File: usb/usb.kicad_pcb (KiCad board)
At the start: 4 copper layers, 40 x 17.5 mm, 14 parts, among them J101 JAE_DX07S016JA3, J102 2x05_Horizontal

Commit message: Update usb + link-poe
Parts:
- C101: footprint Capacitor_SMD:C_0603_1608Metric -> V2_Capacitor_SMD:C_0603
- R101, R102: footprint Resistor_SMD:R_0603_1608Metric -> V2_Resistor_SMD:R_0603
- moved ICON101 13.6 mm to (139.5, 102.2)
- moved H102 5.01 mm to (148.0, 106.2)
- moved J102 5.01 mm to (153.0, 106.2)
- moved PLUG101 5.01 mm to (153.0, 106.2)
- moved FID103 5.00 mm to (161.0, 114.0)
- moved INFO101 3.50 mm to (124.5, 114.2)
- moved INFO102 2.51 mm to (139.5, 113.5)
- moved C101 2.50 mm to (139.5, 106.2)
- moved H101 0.25 mm to (131.0, 106.2)
- moved J101 0.25 mm to (122.0, 106.2)
- moved R101 0.25 mm to (129.0, 101.5)
- moved R102 0.25 mm to (129.0, 111.0)
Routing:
- net /USB+: track 24.5 -> 30.3 mm
- net /USB-: track 31.2 -> 36.7 mm
- net GND: vias 10 -> 29
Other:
- board size 40 x 17.5 mm -> 45 x 17.5 mm

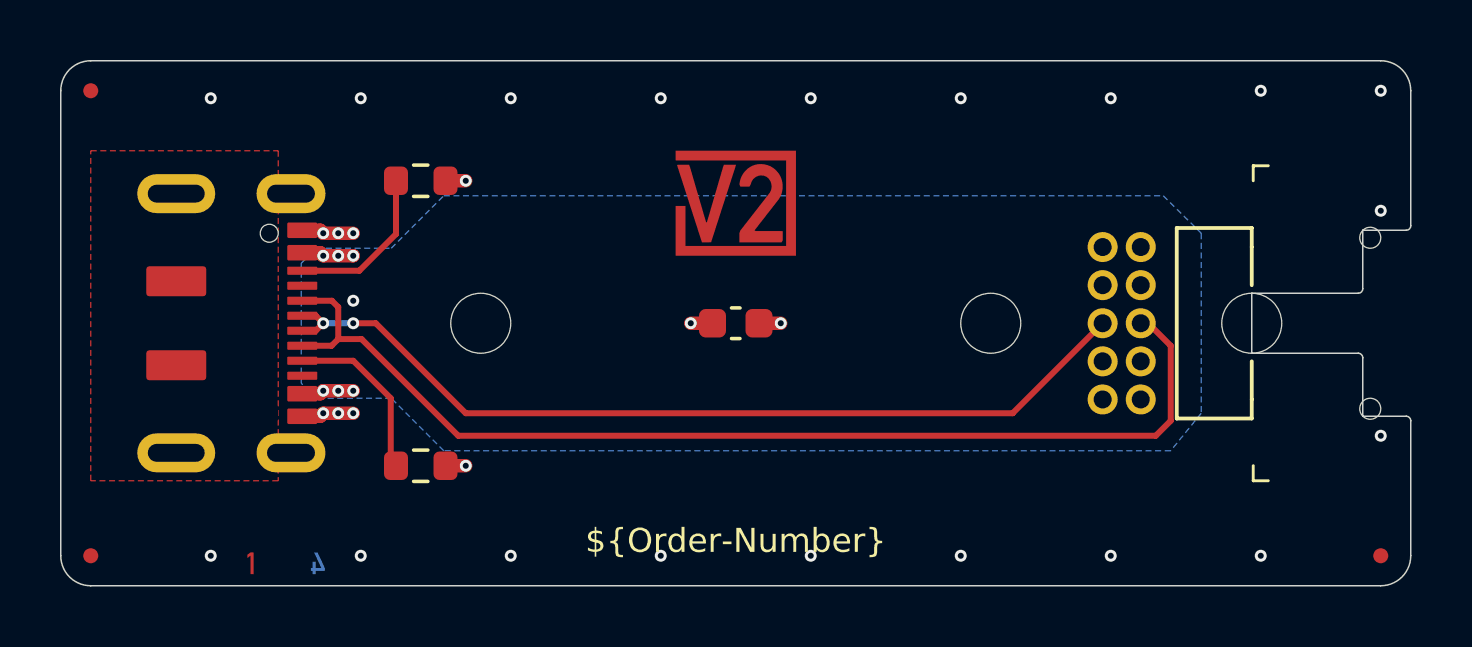
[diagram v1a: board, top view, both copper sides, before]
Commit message: Update power symbols
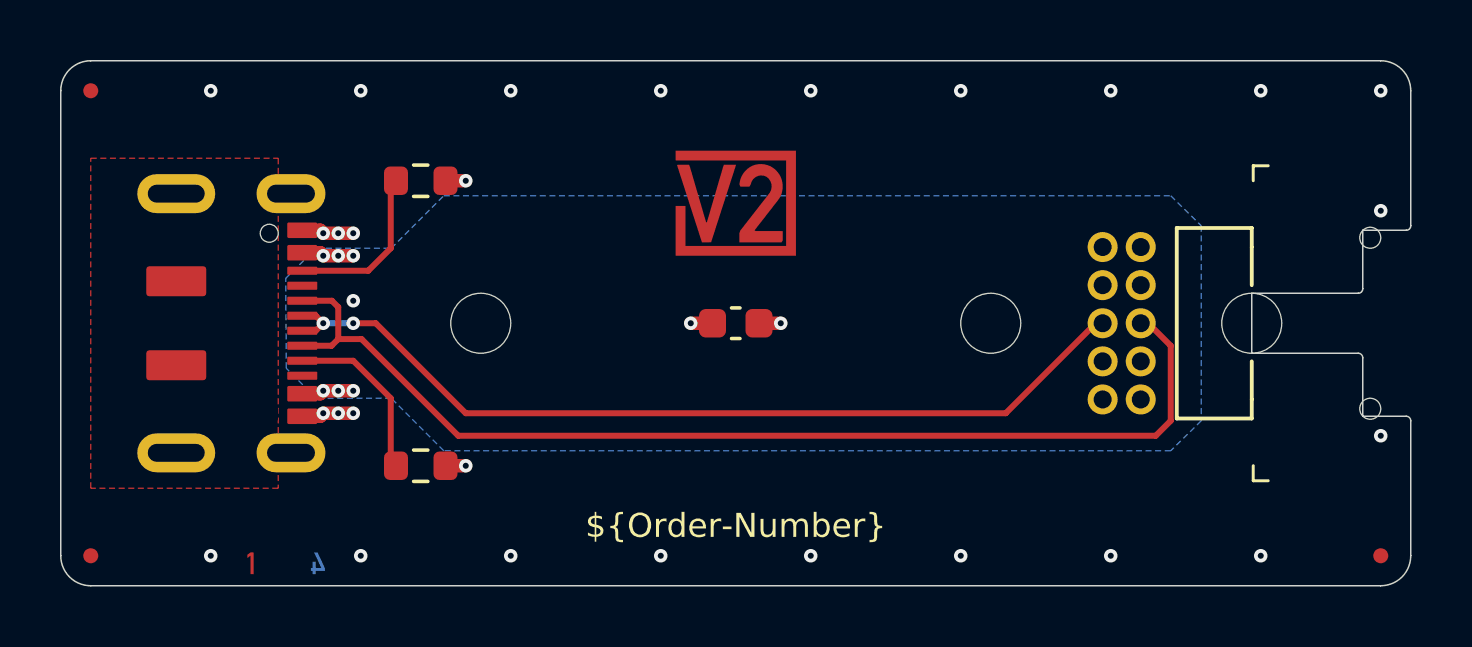
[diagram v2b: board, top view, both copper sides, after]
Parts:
- FID101, FID102, FID103: value Fiducial -> Fiducial_Paste
- INFO102: value ORDER-NUMBER -> Order_Number
- J101: value JAE_DX07S016JA3 -> DX07S016JA3
- moved INFO102 0.50 mm to (139.5, 113.0)
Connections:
- net USB-Shield renamed Shield

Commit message: Fix WAGOs
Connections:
- net VBUS renamed +VBUS
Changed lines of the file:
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@@
 	(net 0 "")
 	(net 1 "GND")
-	(net 2 "VBUS")
+	(net 2 "+VBUS")
 	(net 3 "unconnected-(J101-SBU1-PadA8)")
 	(net 4 "unconnected-(J101-SBU2-PadB8)")
@@
 		)
 		(fp_rect
-			(start -1.48 -0.73)
-			(end 1.48 0.73)
+			(start -1.23 -0.73)
+			(end 1.23 0.73)
 			(stroke
 				(width 0.05)
@@
 		)
 		(pad "1" smd roundrect
-			(at -0.825 0)
-			(size 0.8 0.95)
+			(at -0.75 0)
+			(size 0.75 0.95)
 			(layers "F.Cu" "F.Mask" "F.Paste")
-			(roundrect_rratio 0.25)
+			(roundrect_rratio 0.1333333333)
 			(net 9 "/USB-CC2")
 			(pintype "passive")
 		)
 		(pad "2" smd roundrect
-			(at 0.825 0)
-			(size 0.8 0.95)
+			(at 0.75 0)
+			(size 0.75 0.95)
 			(layers "F.Cu" "F.Mask" "F.Paste")
-			(roundrect_rratio 0.25)
+			(roundrect_rratio 0.1333333333)
 			(net 1 "GND")
 			(pintype "passive")
@@
 			)
 		)
+		(pad "" smd roundrect
+			(at -3.1 -3.05 270)
+			(size 0.45 1)
+			(layers "F.Paste")
+			(roundrect_rratio 0.1)
+		)
 		(pad "" np_thru_hole circle
 			(at -3 -1.95 270)
@@
 			(layers "*.Cu" "*.Mask")
 		)
+		(pad "" smd roundrect
+			(at -2.35 -3.05 270)
+			(size 0.45 1)
+			(layers "F.Paste")
+			(roundrect_rratio 0.1)
+		)
+		(pad "" smd roundrect
+			(at 2.35 -3.05 270)
+			(size 0.45 1)
+			(layers "F.Paste")
+			(roundrect_rratio 0.1)
+		)
 		(pad "" np_thru_hole oval
 			(at 3 -1.95 270)
@@
 			(layers "*.Cu" "*.Mask")
 		)
+		(pad "" smd roundrect
+			(at 3.1 -3.05 270)
+			(size 0.45 1)
+			(layers "F.Paste")
+			(roundrect_rratio 0.1)
+		)
 		(pad "A5" smd roundrect
 			(at -1.75 -3.05 270)
@@
 			(at -3.1 -3.05 270)
 			(size 0.52 1)
-			(layers "F.Cu" "F.Mask" "F.Paste")
+			(layers "F.Cu" "F.Mask")
 			(roundrect_rratio 0.1)
 			(net 1 "GND")
@@
 			(at 3.1 -3.05 270)
 			(size 0.52 1)
-			(layers "F.Cu" "F.Mask" "F.Paste")
+			(layers "F.Cu" "F.Mask")
 			(roundrect_rratio 0.1)
 			(net 1 "GND")
@@
 			(at -2.35 -3.05 270)
 			(size 0.52 1)
-			(layers "F.Cu" "F.Mask" "F.Paste")
+			(layers "F.Cu" "F.Mask")
 			(roundrect_rratio 0.1)
-			(net 2 "VBUS")
+			(net 2 "+VBUS")
 			(pinfunction "VBUS")
 			(pintype "passive")
@@
 			(at 2.35 -3.05 270)
 			(size 0.52 1)
-			(layers "F.Cu" "F.Mask" "F.Paste")
+			(layers "F.Cu" "F.Mask")
 			(roundrect_rratio 0.1)
-			(net 2 "VBUS")
+			(net 2 "+VBUS")
 			(pinfunction "VBUS")
 			(pintype "passive")
@@
 		)
 		(fp_rect
-			(start -1.48 -0.73)
-			(end 1.48 0.73)
+			(start -1.23 -0.73)
+			(end 1.23 0.73)
 			(stroke
 				(width 0.05)
@@
 		)
 		(pad "1" smd roundrect
-			(at -0.775 0 180)
-			(size 0.9 0.95)
+			(at -0.7 0 180)
+			(size 0.7 0.8)
 			(layers "F.Cu" "F.Mask" "F.Paste")
-			(roundrect_rratio 0.25)
-			(net 2 "VBUS")
+			(roundrect_rratio 0.1428571429)
+			(net 2 "+VBUS")
 			(pintype "passive")
 		)
 		(pad "2" smd roundrect
-			(at 0.775 0 180)
-			(size 0.9 0.95)
+			(at 0.7 0 180)
+			(size 0.7 0.8)
 			(layers "F.Cu" "F.Mask" "F.Paste")
-			(roundrect_rratio 0.25)
+			(roundrect_rratio 0.1428571429)
 			(net 1 "GND")
 			(pintype "passive")
@@
 		)
 		(fp_rect
-			(start -1.48 -0.73)
-			(end 1.48 0.73)
+			(start -1.23 -0.73)
+			(end 1.23 0.73)
 			(stroke
 				(width 0.05)
@@
 		)
 		(pad "1" smd roundrect
-			(at -0.825 0)
-			(size 0.8 0.95)
+			(at -0.75 0)
+			(size 0.75 0.95)
 			(layers "F.Cu" "F.Mask" "F.Paste")
-			(roundrect_rratio 0.25)
+			(roundrect_rratio 0.1333333333)
 			(net 8 "/USB-CC1")
 			(pintype "passive")
 		)
 		(pad "2" smd roundrect
-			(at 0.825 0)
-			(size 0.8 0.95)
+			(at 0.75 0)
+			(size 0.75 0.95)
 			(layers "F.Cu" "F.Mask" "F.Paste")
-			(roundrect_rratio 0.25)
+			(roundrect_rratio 0.1333333333)
 			(net 1 "GND")
 			(pintype "passive")
@@
 			(keep_end_layers yes)
 			(zone_layer_connections)
-			(net 2 "VBUS")
+			(net 2 "+VBUS")
 			(pinfunction "Pin_4")
 			(pintype "passive")
@@
 			(keep_end_layers yes)
 			(zone_layer_connections)
-			(net 2 "VBUS")
+			(net 2 "+VBUS")
 			(pinfunction "Pin_7")
 			(pintype "passive")
@@
 	(zone
 		(net 2)
-		(net_name "VBUS")
+		(net_name "+VBUS")
 		(layer "B.Cu")
 		(hatch edge 0.5)

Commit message: Refresh
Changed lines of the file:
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@@
 			(effects
 				(font
-					(size 0.75 0.75)
+					(size 0.5 0.5)
 					(thickness 0.1)
 				)
@@
 		)
 		(fp_line
-			(start -3.175 -1.2)
-			(end -3.175 -3.7)
-			(stroke
-				(width 0.127)
-				(type solid)
-			)
-			(layer "F.SilkS")
-		)
-		(fp_line
 			(start 3.175 -1.2)
 			(end -3.175 -1.2)
 			(stroke
-				(width 0.127)
+				(width 0.1)
 				(type solid)
 			)
@@
 			(end -2.54 -3.7)
 			(stroke
-				(width 0.127)
+				(width 0.1)
 				(type solid)
 			)
@@
 			(end -1.27 -3.7)
 			(stroke
-				(width 0.127)
+				(width 0.1)
 				(type solid)
 			)
@@
 			(end 2.54 -3.7)
 			(stroke
-				(width 0.127)
+				(width 0.1)
 				(type solid)
 			)
@@
 			(end 3.175 -3.7)
 			(stroke
-				(width 0.127)
-				(type solid)
-			)
-			(layer "F.SilkS")
-		)
-		(fp_line
-			(start 3.175 -3.7)
-			(end 3.175 -1.2)
-			(stroke
-				(width 0.127)
-				(type solid)
-			)
+				(width 0.1)
+				(type solid)
+			)
+			(layer "F.SilkS")
+		)
+		(fp_poly
+			(pts
+				(xy 4.01 0.155) (xy 3.77 -0.175) (xy 4.25 -0.175) (xy 4.01 0.155)
+			)
+			(stroke
+				(width 0.12)
+				(type solid)
+			)
+			(fill yes)
 			(layer "F.SilkS")
 		)
@@
 			(effects
 				(font
-					(size 0.75 0.75)
+					(size 0.5 0.5)
 					(thickness 0.1)
 					(bold yes)
@@
 		)
 		(embedded_fonts no)
-		(model "../../3dmodels/V2_Connector_PinHeader_1.27mm.3dshapes/PinHeader_2x05_P1.27mm.stp"
+		(model "../../3dmodels/V2_Connector_PinHeader_1.27mm.3dshapes/PinHeader_2x05_P1.27mm_Horizontal.step"
 			(offset
 				(xyz 2.52 1.18 1.65)
@@
 			)
 		)
-	)
-	(gr_line
-		(start 162 109.5)
-		(end 162 114)
-		(stroke
-			(width 0.05)
-			(type solid)
-		)
-		(layer "Edge.Cuts")
 	)
 	(gr_line
@@
 		(layer "Edge.Cuts")
 	)
+	(gr_arc
+		(start 117 98.5)
+		(mid 117.292893 97.792893)
+		(end 118 97.5)
+		(stroke
+			(width 0.05)
+			(type solid)
+		)
+		(layer "Edge.Cuts")
+	)
 	(gr_line
 		(start 118 97.5)
 		(end 161 97.5)
-		(stroke
-			(width 0.05)
-			(type solid)
-		)
-		(layer "Edge.Cuts")
-	)
-	(gr_line
-		(start 162 98.5)
-		(end 162 103)
 		(stroke
 			(width 0.05)
@@
 		(layer "Edge.Cuts")
 	)
-	(gr_arc
-		(start 162 114)
-		(mid 161.707107 114.707107)
+	(gr_line
+		(start 118 115)
 		(end 161 115)
-		(stroke
-			(width 0.05)
-			(type solid)
-		)
-		(layer "Edge.Cuts")
-	)
-	(gr_arc
-		(start 117 98.5)
-		(mid 117.292893 97.792893)
-		(end 118 97.5)
 		(stroke
 			(width 0.05)
@@
 	)
 	(gr_line
-		(start 118 115)
+		(start 162 98.5)
+		(end 162 103)
+		(stroke
+			(width 0.05)
+			(type solid)
+		)
+		(layer "Edge.Cuts")
+	)
+	(gr_line
+		(start 162 109.5)
+		(end 162 114)
+		(stroke
+			(width 0.05)
+			(type solid)
+		)
+		(layer "Edge.Cuts")
+	)
+	(gr_arc
+		(start 162 114)
+		(mid 161.707107 114.707107)
 		(end 161 115)
 		(stroke

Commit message: Replace Order_Number
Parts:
- H101, H102: value MountingHole_2mm -> 2mm
- INFO102: value Order_Number -> ~; footprint V2_Production:Order_Number -> V2_Production:Revision

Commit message: Export stencil
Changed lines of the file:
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@@
 	(paper "A4")
 	(title_block
-		(date "2026-02-10")
+		(date "2026-02-25")
 		(rev "2026-01-12")
 	)
@@
 			)
 		)
-		(property "Description" "Resistor, small symbol"
+		(property "Description" ""
 			(at 0 0 0)
 			(layer "F.Fab")
@@
 			)
 		)
-		(property "Description" "Fiducial Marker"
+		(property "Description" ""
 			(at 0 0 0)
 			(unlocked yes)
@@
 			)
 		)
-		(property "Description" "Unpolarized capacitor, small symbol"
+		(property "Description" ""
 			(at 0 0 180)
 			(layer "F.Fab")
@@
 			)
 		)
-		(property "Description" "Fiducial Marker"
+		(property "Description" ""
 			(at 0 0 0)
 			(unlocked yes)
@@
 			)
 		)
-		(property "Description" "Resistor, small symbol"
+		(property "Description" ""
 			(at 0 0 0)
 			(layer "F.Fab")
@@
 			)
 		)
-		(property "Description" "Mounting Hole without connection"
+		(property "Description" ""
 			(at 0 0 0)
 			(unlocked yes)
@@
 			)
 		)
-		(property "Description" "Mounting Hole without connection"
+		(property "Description" ""
 			(at 0 0 0)
 			(unlocked yes)
@@
 			)
 		)
-		(property "Description" "Fiducial Marker"
+		(property "Description" ""
 			(at 0 0 0)
 			(unlocked yes)
@@
 			)
 		)
-		(property "Description" "Amphenol – Minitek127"
+		(property "Description" ""
 			(at 0 0 270)
 			(unlocked yes)
